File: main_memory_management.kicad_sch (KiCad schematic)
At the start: 19 parts

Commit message: Notes and minor fixes
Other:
- note added: "ALT RAM ROM VIDEO RAM"
- note removed: "RAM RAM RAM ALT RAM ROM VIDEO RAM RAM RAM"
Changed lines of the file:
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@@
     (effects (font (size 1.27 1.27)) (justify left bottom))
   )
-  (text "RAM\nRAM\nRAM\nALT RAM\nROM\nVIDEO RAM\nRAM\nRAM" (at 172.72 53.34 0)
+  (text "\n\n\nALT RAM\nROM\nVIDEO RAM" (at 172.72 48.26 0)
     (effects (font (size 1.6 1.6)) (justify left bottom))
   )
@@
   (symbol (lib_id "Device:R") (at 62.23 168.91 270) (unit 1)
     (in_bom yes) (on_board yes) (dnp no) (fields_autoplaced)
-    (property "Reference" "R2" (at 62.23 163.83 90)
-      (effects (font (size 1.27 1.27)))
-    )
-    (property "Value" "R" (at 62.23 166.37 90)
-      (effects (font (size 1.27 1.27)))
-    )
+    (property "Reference" "R2" (at 62.23 172.72 90)
+      (effects (font (size 1.27 1.27)))
+    )
+    (property "Value" "R" (at 62.23 175.26 90)
+      (effects (font (size 1.27 1.27)))
+    )

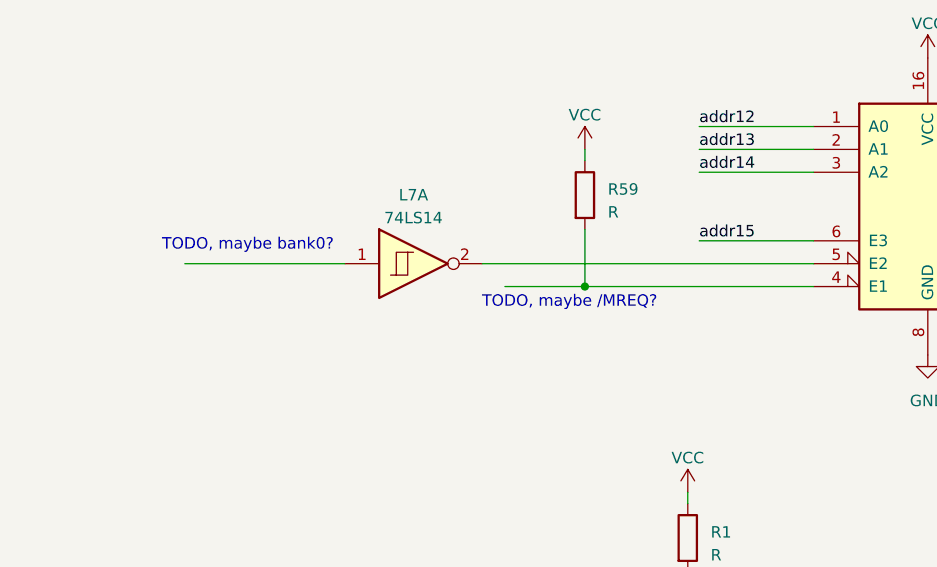
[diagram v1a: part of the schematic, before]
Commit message: Discovered bank 0 + fixed wrong signals in video gen
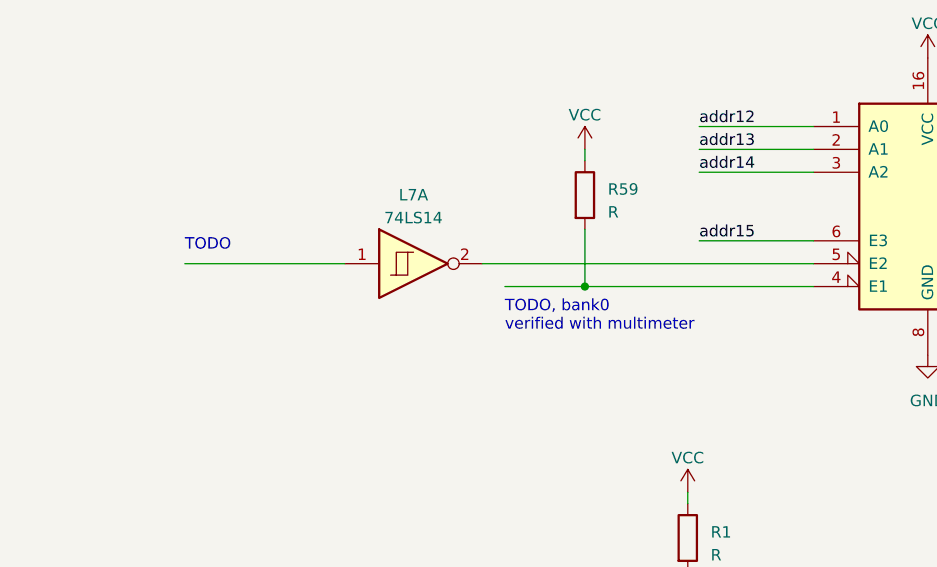
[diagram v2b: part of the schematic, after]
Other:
- note added: "TODO, bank0 verified with multimeter"
- note removed: "TODO, maybe /MREQ?"
- note removed: "TODO, maybe bank0?"
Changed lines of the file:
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@@
     (effects (font (size 1.27 1.27)) (justify left bottom))
   )
-  (text "TODO, maybe /MREQ?" (at 73.66 55.88 0)
+  (text "TODO, bank0\nverified with multimeter" (at 76.2 58.42 0)
     (effects (font (size 1.27 1.27)) (justify left bottom))
   )
-  (text "TODO, maybe bank0?" (at 38.1 49.53 0)
+  (text "TODO" (at 40.64 49.53 0)
     (effects (font (size 1.27 1.27)) (justify left bottom))
   )

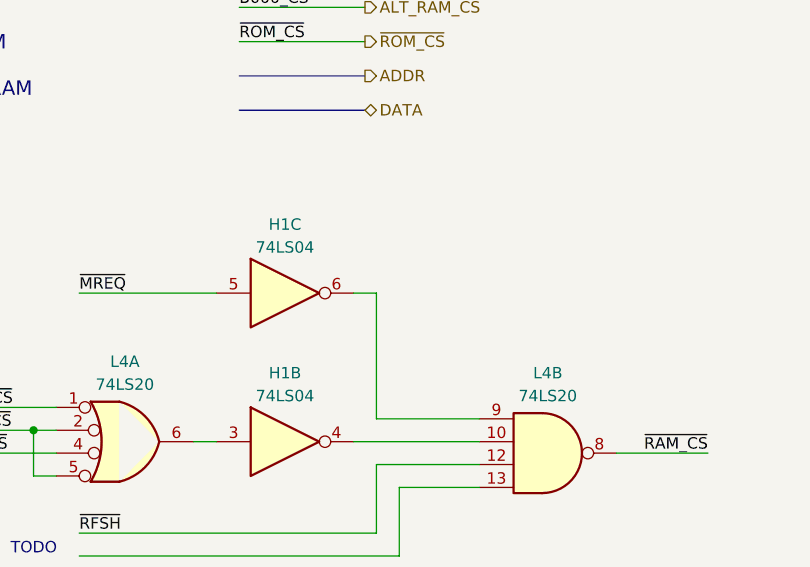
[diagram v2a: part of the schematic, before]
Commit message: Added some missing labels and references
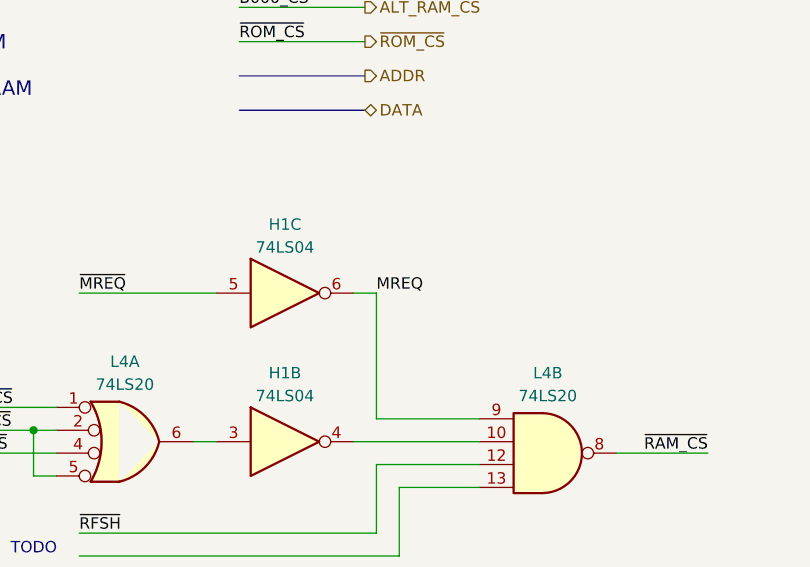
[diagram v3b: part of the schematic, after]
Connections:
- net MREQ: now reaches H1.6, L4.9
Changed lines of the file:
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@@
     (effects (font (size 1.27 1.27)) (justify right bottom))
+  )
+  (label "MREQ" (at 223.52 69.85 0) (fields_autoplaced)
+    (effects (font (size 1.27 1.27)) (justify left bottom))
   )
   (hierarchical_label "~{RESET}" (shape input) (at 27.94 105.41 180) (fields_autoplaced)

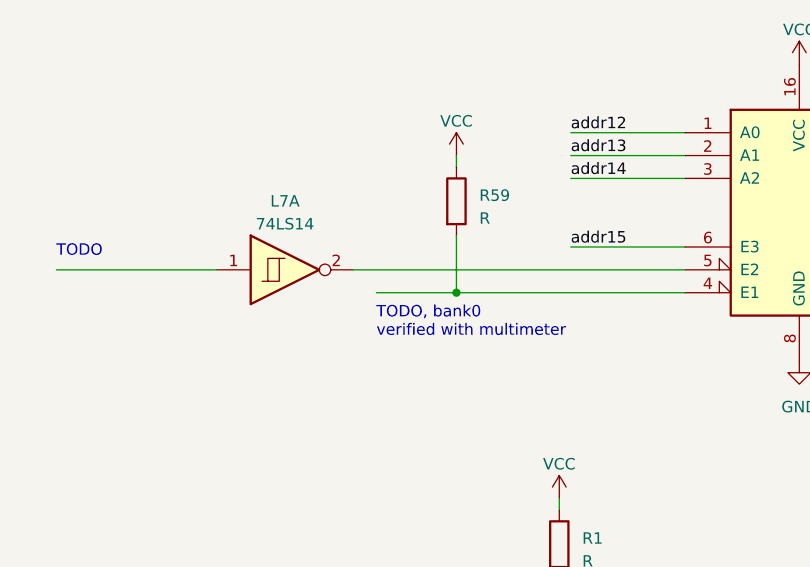
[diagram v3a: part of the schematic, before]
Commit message: Added FDC sheet (WIP), added partial parallel port inout
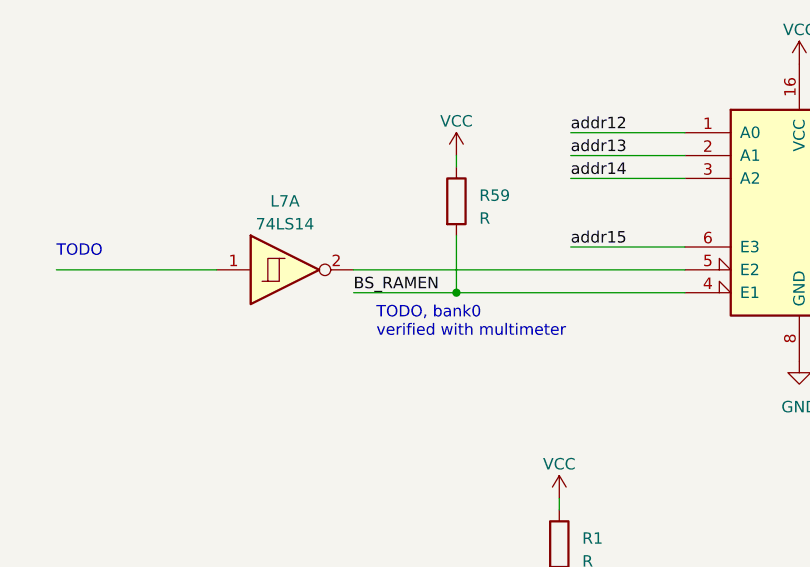
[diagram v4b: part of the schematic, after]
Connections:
- net BS_RAMEN: now reaches L2.4 (E1), R59.2
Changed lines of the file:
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@@
     (stroke (width 0) (type default))
   )
-  (wire (pts (xy 76.2 53.34) (xy 85.09 53.34))
+  (wire (pts (xy 73.66 53.34) (xy 85.09 53.34))
     (stroke (width 0) (type default))
   )
@@
     (effects (font (size 1.27 1.27)) (justify left bottom))
   )
+  (label "BS_RAMEN" (at 73.66 53.34 0) (fields_autoplaced)
+    (effects (font (size 1.27 1.27)) (justify left bottom))
+  )

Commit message: Removed some dangling notes
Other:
- note removed: "TODO, bank0 verified with multimeter"
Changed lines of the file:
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@@
-    (effects (font (size 1.27 1.27)) (justify left bottom))
-  )
-  (text "TODO, bank0\nverified with multimeter" (at 76.2 58.42 0)
     (effects (font (size 1.27 1.27)) (justify left bottom))
   )

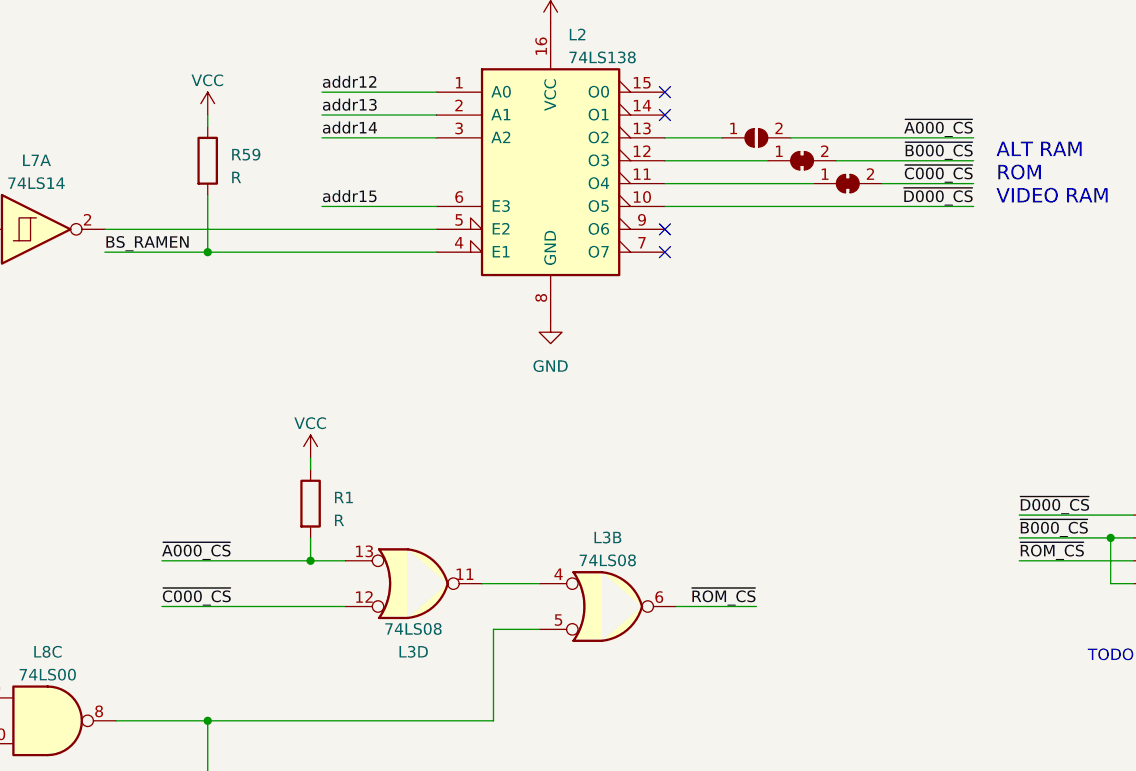
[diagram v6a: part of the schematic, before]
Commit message: GPIO: wire renaming
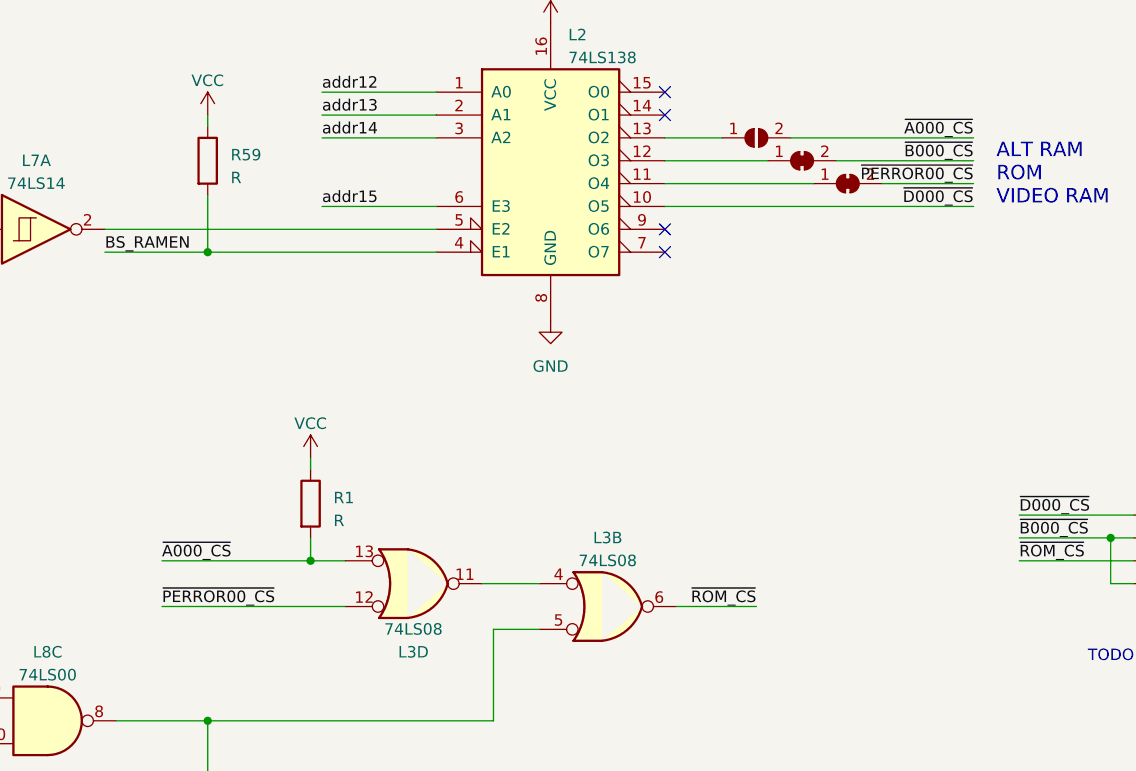
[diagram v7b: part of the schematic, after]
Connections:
- net ~{C000_CS} renamed ~{PERROR00_CS}
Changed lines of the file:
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@@
     (effects (font (size 1.27 1.27)) (justify right bottom))
   )
-  (label "~{C000_CS}" (at 80.01 92.71 0) (fields_autoplaced)
+  (label "~{PERROR00_CS}" (at 80.01 92.71 0) (fields_autoplaced)
     (effects (font (size 1.27 1.27)) (justify left bottom))
   )
@@
     (effects (font (size 1.27 1.27)) (justify right bottom))
   )
-  (label "~{C000_CS}" (at 170.18 45.72 180) (fields_autoplaced)
+  (label "~{PERROR00_CS}" (at 170.18 45.72 180) (fields_autoplaced)
     (effects (font (size 1.27 1.27)) (justify right bottom))
   )

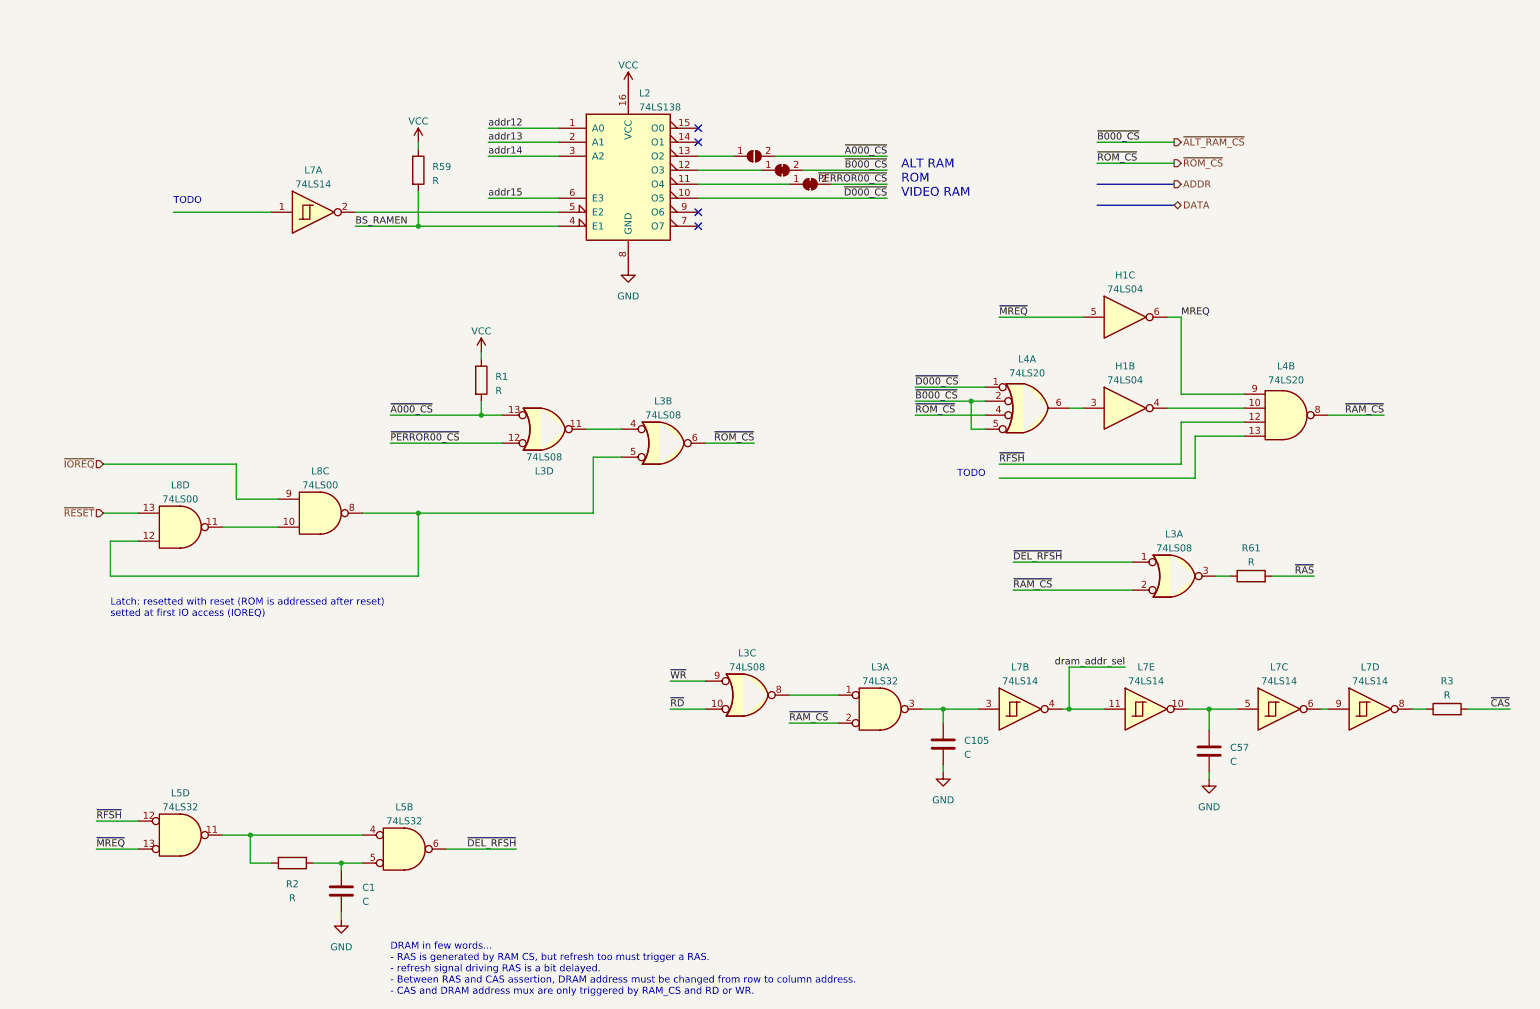
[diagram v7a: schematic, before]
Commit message: MainMemoryManagement: wire renaming
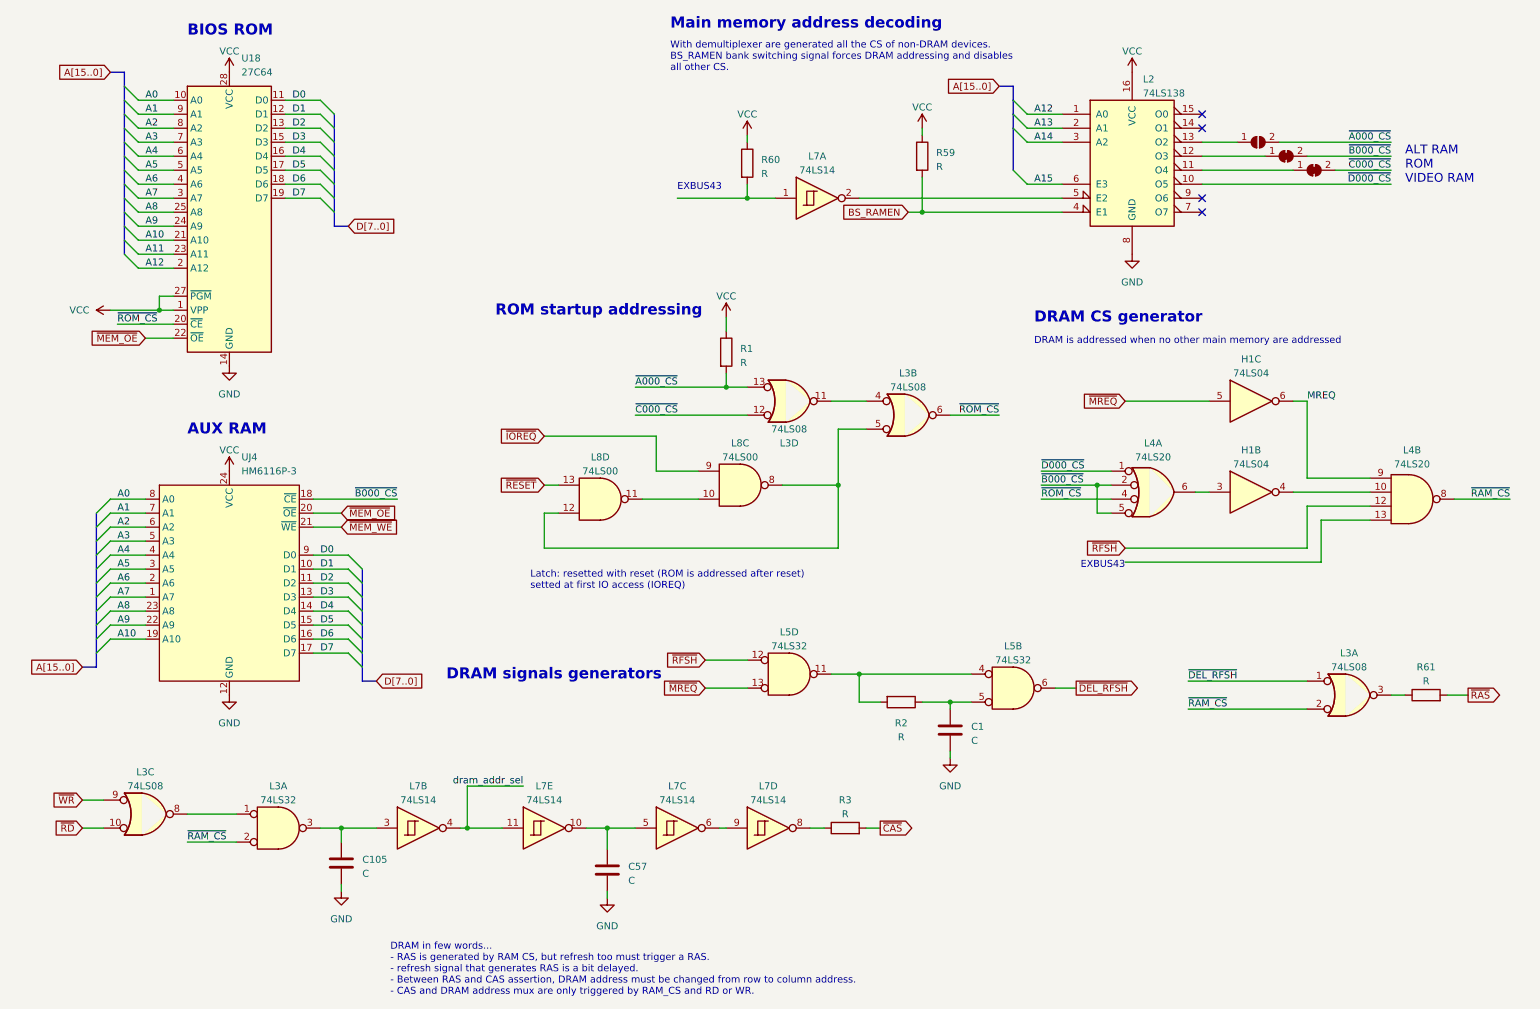
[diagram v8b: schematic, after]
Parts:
- added R60: R, symbol Device:R
- added U18: 27C64, Package_DIP:DIP-28_W15.24mm, symbol Memory_EPROM:27C64
- added UJ4: HM6116P-3, symbol ceda:uPD446
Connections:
- net GND: now also U18.14 (GND), UJ4.12 (GND)
- net VCC: now also R60.1, U18.1 (VPP), U18.27 (~{PGM}), U18.28 (VCC), UJ4.24 (VCC)
- net ~{ROM_CS}: now also U18.20 (~{CE})
- net at L7.1: now also R60.2
- net addr12 renamed A12
- net A12: now also U18.2 (A12)
- net addr13 renamed A13
- net addr14 renamed A14
- net addr15 renamed A15
- net ~{ALT_RAM_CS} renamed ~{B000_CS}
- net ~{B000_CS}: now also UJ4.18 (~{CE})
- net ~{PERROR00_CS} renamed ~{C000_CS}
- new net A0: U18.10 (A0), UJ4.8 (A0)
- new net A1: U18.9 (A1), UJ4.7 (A1)
- new net A10: U18.21 (A10), UJ4.19 (A10)
- new net A11: U18.23 (A11)
- new net A2: U18.8 (A2), UJ4.6 (A2)
- new net A3: U18.7 (A3), UJ4.5 (A3)
- new net A4: U18.6 (A4), UJ4.4 (A4)
- new net A5: U18.5 (A5), UJ4.3 (A5)
- new net A6: U18.4 (A6), UJ4.2 (A6)
- new net A7: U18.3 (A7), UJ4.1 (A7)
- new net A8: U18.25 (A8), UJ4.23 (A8)
- new net A9: U18.24 (A9), UJ4.22 (A9)
- new net D0: U18.11 (D0), UJ4.9 (D0)
- new net D1: U18.12 (D1), UJ4.10 (D1)
- new net D2: U18.13 (D2), UJ4.11 (D2)
- new net D3: U18.15 (D3), UJ4.13 (D3)
- new net D4: U18.16 (D4), UJ4.14 (D4)
- new net D5: U18.17 (D5), UJ4.15 (D5)
- new net D6: U18.18 (D6), UJ4.16 (D6)
- new net D7: U18.19 (D7), UJ4.17 (D7)
- new net ~{MEM_OE}: U18.22 (~{OE}), UJ4.20 (~{OE})
- new net ~{MEM_WE}: UJ4.21 (~{WE})
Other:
- note added: "AUX RAM"
- note added: "BIOS ROM"
- note added: "DRAM CS generator"
- note added: "DRAM in few words... - RAS is generated by RAM CS, but refresh too must trigger a RAS. - refresh signal that generates RAS is a bit delayed. - Between RAS and CAS assertion, DRAM address must be changed from row to column address. - CAS and DRAM address mux are only triggered by RAM_CS and RD or WR."
- note added: "DRAM is addressed when no other main memory are addressed"
- note added: "DRAM signals generators"
- note added: "EXBUS43"
- note added: "Main memory address decoding"
- note added: "ROM startup addressing"
- note added: "With demultiplexer are generated all the CS of non-DRAM devices. BS_RAMEN bank switching signal forces DRAM addressing and disables all other CS."
- note removed: "DRAM in few words... - RAS is generated by RAM CS, but refresh too must trigger a RAS. - refresh signal driving RAS is a bit delayed. - Between RAS and CAS assertion, DRAM address must be changed from row to column address. - CAS and DRAM address mux are only triggered by RAM_CS and RD or WR."
- note removed: "TODO"
- moved on the sheet: C1, C105, C57, H1B, H1C, L2, L3A, L3B, L3C, L3D, L4A, L4B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
